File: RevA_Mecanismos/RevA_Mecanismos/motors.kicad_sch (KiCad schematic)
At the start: 46 parts, among them U4 TXU0304PWR, U6 SRV05-4

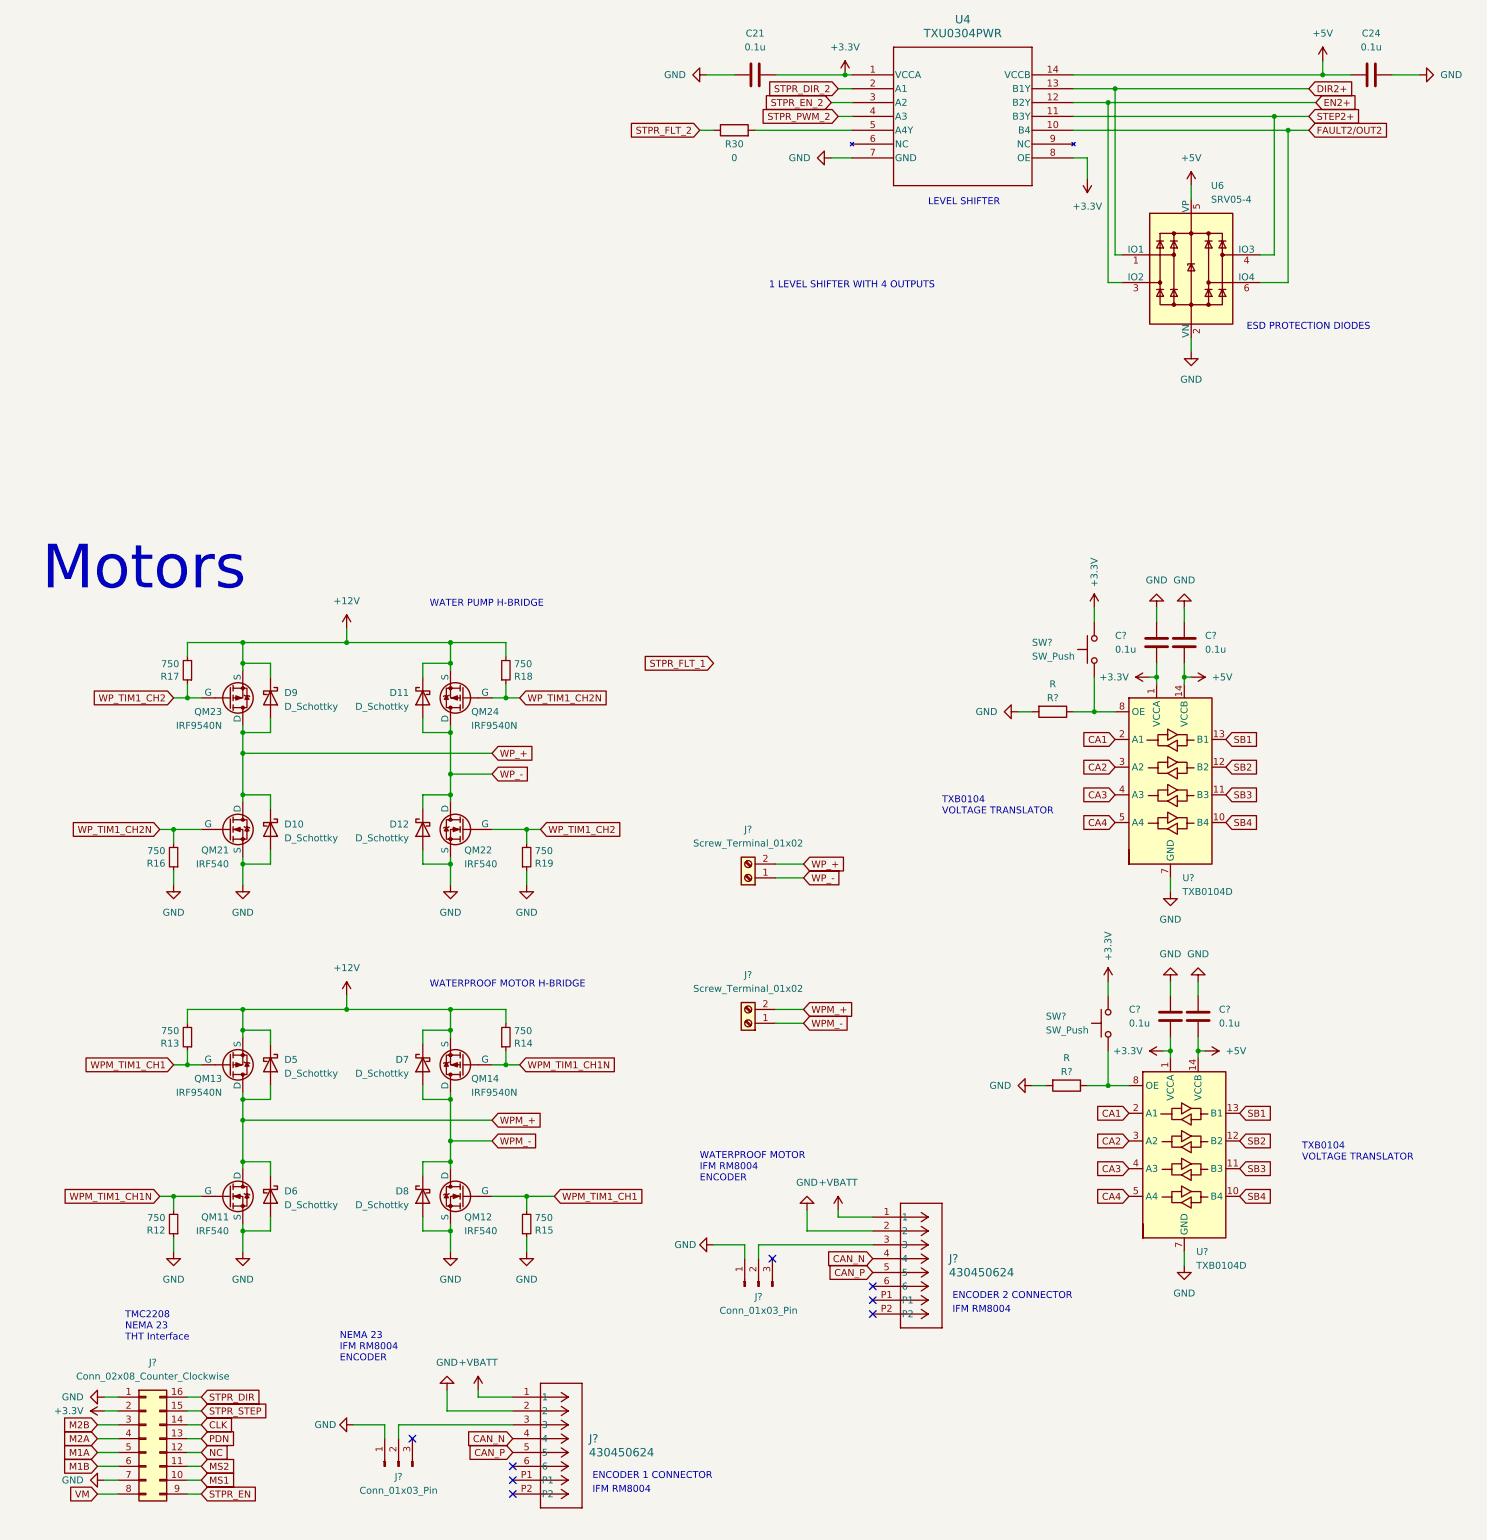
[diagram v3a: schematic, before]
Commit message: Debug connectors and pwr flag to +12v
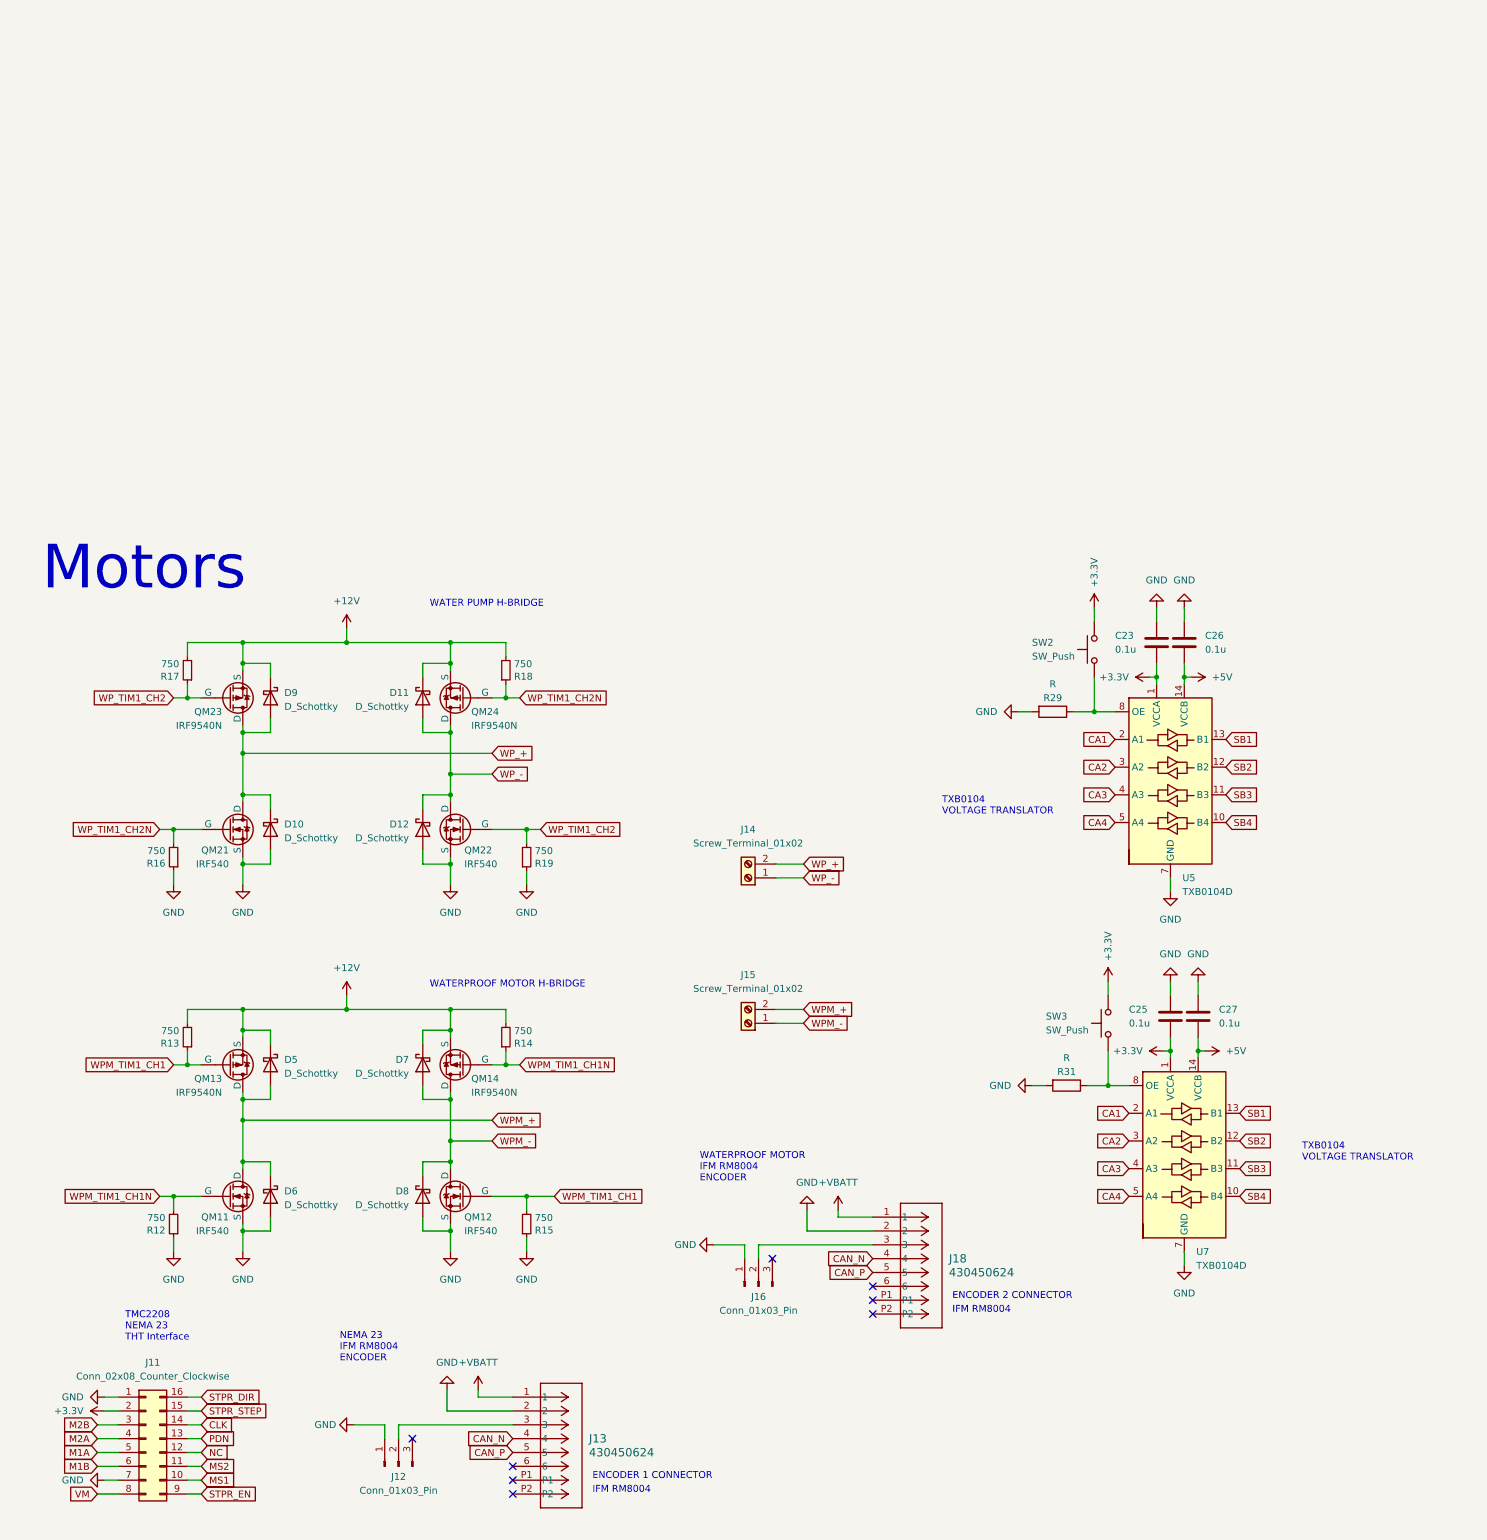
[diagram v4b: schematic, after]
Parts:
- removed C21, C24: 0.1u, symbol Device:C
- removed R30: 0, symbol Device:R
- removed U4: TXU0304PWR, TSSOP14_PW_TEX, symbol TXU0304PWR:TXU0304PWR
- removed U6: SRV05-4, Package_TO_SOT_SMD:SOT-23-6, symbol Power_Protection:SRV05-4
- gave numbers to parts that had none: 17
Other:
- note removed: "1 LEVEL SHIFTER WITH 4 OUTPUTS"
- note removed: "ESD PROTECTION DIODES"
- note removed: "LEVEL SHIFTER"

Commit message: Updated STM32 USV Mechanism PCB
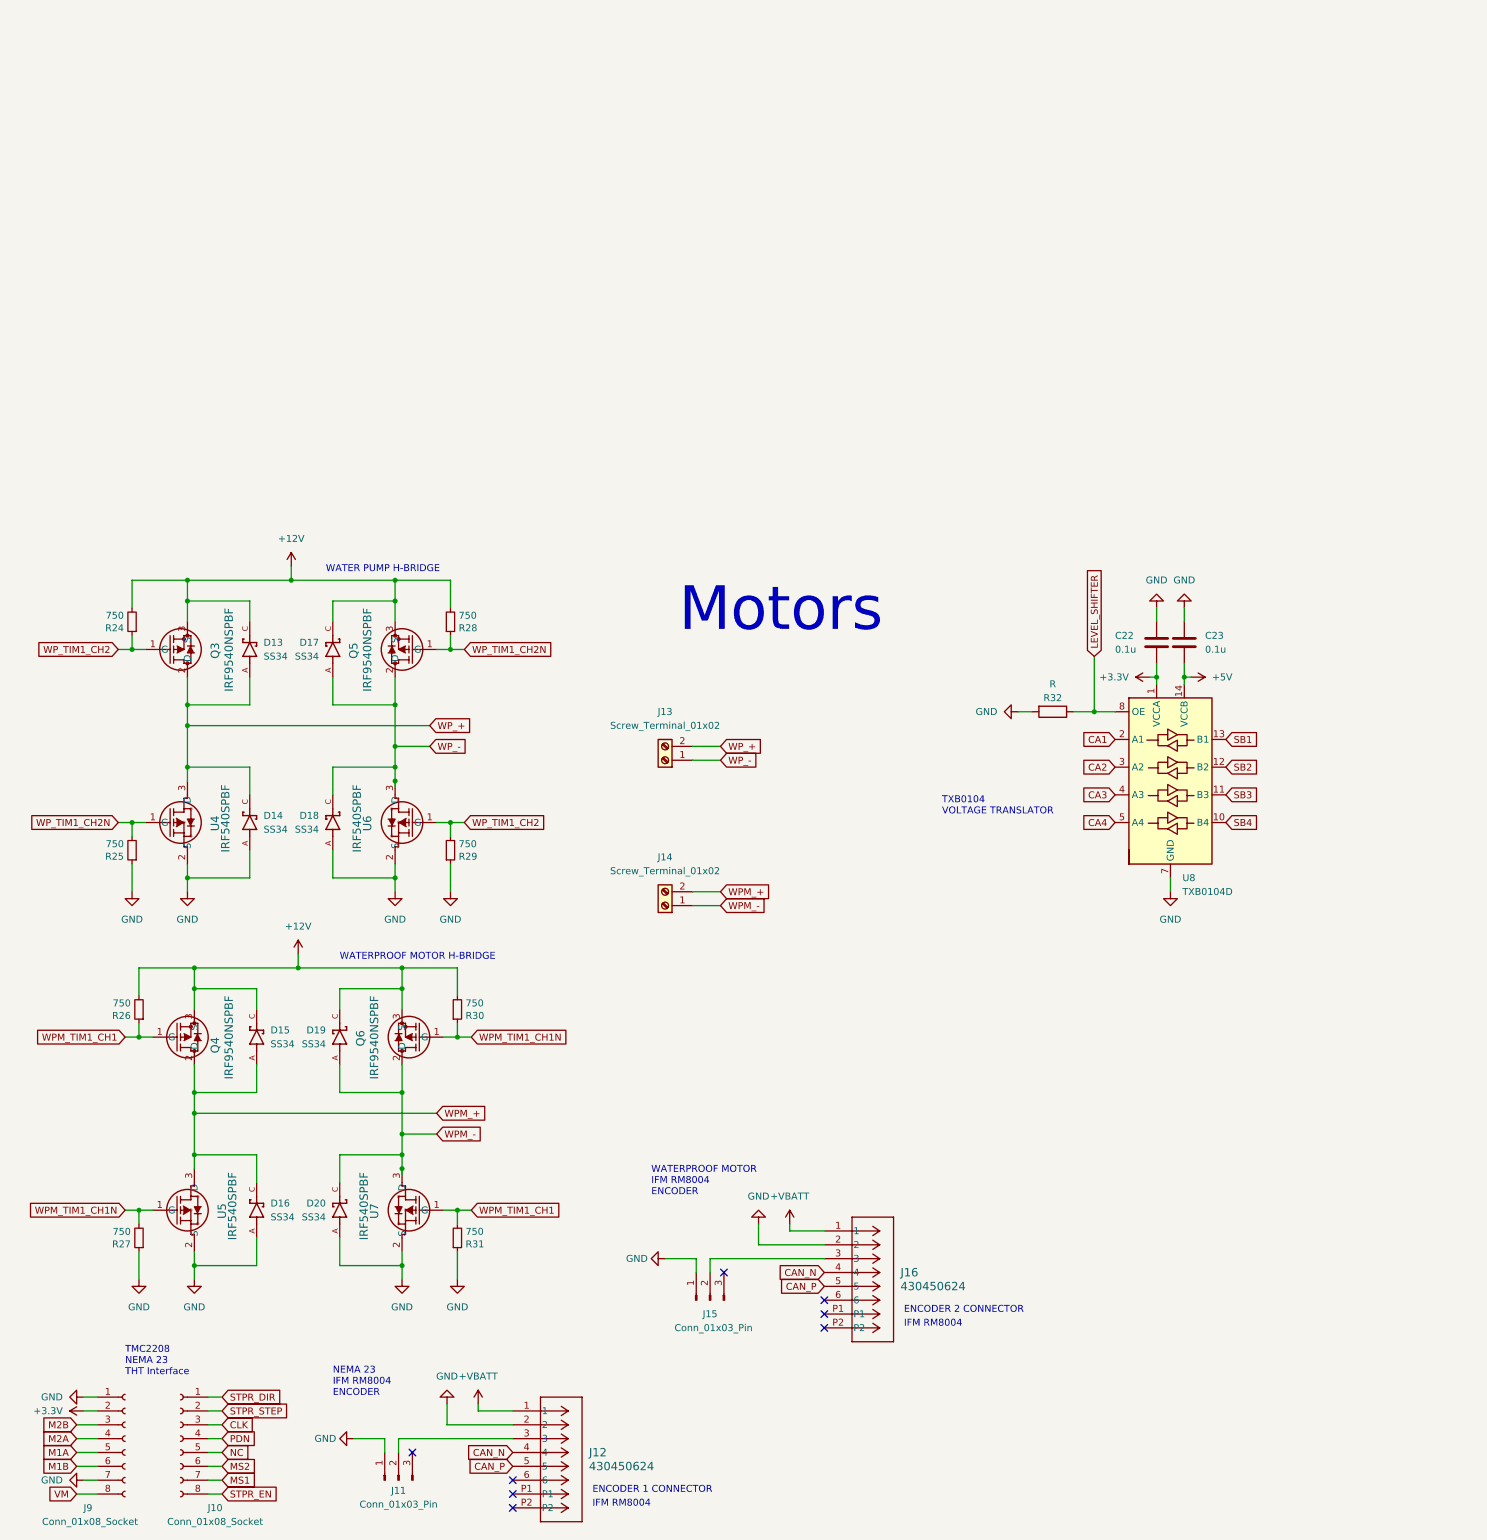
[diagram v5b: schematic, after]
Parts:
- removed C25, C27: 0.1u, symbol Device:C
- removed D10, D11, D12, D5, D6, D7, D8, D9: D_Schottky, symbol Device:D_Schottky
- removed J11: Conn_02x08_Counter_Clockwise, Connector_PinHeader_2.54mm:PinHeader_2x08_P2.54mm_Vertical, symbol Connector_Generic:Conn_02x08_Counter_Clockwise
- removed QM11, QM12, QM21, QM22: IRF540, symbol Simulation_SPICE:NMOS
- removed QM13, QM14, QM23, QM24: IRF9540N, symbol Simulation_SPICE:PMOS
- removed R12, R13, R14, R15, R16, R17, R18, R19: 750, Resistor_SMD:R_0603_1608Metric, symbol Device:R_Small
- removed R31: R, symbol Device:R
- removed SW2, SW3: SW_Push, symbol Switch:SW_Push
- removed U7: TXB0104D, Package_SO:SOIC-14_3.9x8.7mm_P1.27mm, symbol Logic_LevelTranslator:TXB0104D
- added D13, D14, D15, D16, D17, D18, D19, D20: SS34, SS34:SS34, symbol SS34:SS34
- added J10, J9: Conn_01x08_Socket, Connector_PinSocket_2.54mm:PinSocket_1x08_P2.54mm_Vertical, symbol Connector:Conn_01x08_Socket
- added Q3, Q4, Q5, Q6: IRF9540NSPBF, PMOSGDS_D2PAK_INF, symbol IRF9540NSPBF:IRF9540NSPBF
- added R24, R25, R26, R27, R28, R29, R30, R31: 750, Resistor_SMD:R_0603_1608Metric, symbol Device:R_Small
- added U4, U5, U6, U7: IRF540SPBF, D2PAK_VIS, symbol IRF540SPBF:IRF540SPBF
- C22: renamed from C23; footprint (none) -> Capacitor_SMD:C_0603_1608Metric
- C23: renamed from C26; footprint (none) -> Capacitor_SMD:C_0603_1608Metric
- J11: renamed from J12; footprint (none) -> Connector_PinHeader_2.54mm:PinHeader_1x03_P2.54mm_Vertical
- J12: renamed from J13; footprint CON_430450624_MOL -> MolexConnectors:CON_430450624_MOL
- J15: renamed from J16; footprint (none) -> Connector_PinHeader_2.54mm:PinHeader_1x03_P2.54mm_Vertical
- J16: renamed from J18; footprint CON_430450624_MOL -> MolexConnectors:CON_430450624_MOL
- R32: renamed from R29; footprint (none) -> Resistor_SMD:R_0603_1608Metric
- renumbered J14 to J13, J15 to J14, U5 to U8
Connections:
- net +12V: now also D13.C, D15.C, D17.C, D19.C, Q3.3 (S), Q4.3 (S), Q5.3 (S), Q6.3 (S), R24.2, R26.2, R28.2, R30.2
- net +3.3V: now also J9.2 (Pin_2)
- net CLK: now also J10.3 (Pin_3)
- net GND: now also D14.A, D16.A, D18.A, D20.A, J9.1 (Pin_1), J9.7 (Pin_7), R25.1, R27.1, R29.1, R31.1, U4.2 (S), U5.2 (S), U6.2 (S), U7.2 (S)
- net M1A: now also J9.5 (Pin_5)
- net M1B: now also J9.6 (Pin_6)
- net M2A: now also J9.4 (Pin_4)
- net M2B: now also J9.3 (Pin_3)
- net MS1: now also J10.7 (Pin_7)
- net MS2: now also J10.6 (Pin_6)
- net NC: now also J10.5 (Pin_5)
- net PDN: now also J10.4 (Pin_4)
- net STPR_DIR: now also J10.1 (Pin_1)
- net STPR_EN: now also J10.8 (Pin_8)
- net STPR_STEP: now also J10.2 (Pin_2)
- net VM: now also J9.8 (Pin_8)
- net WPM_+: now also D15.A, D16.C, Q4.2 (D), U5.3 (D)
- net WPM_-: now also D19.A, D20.C, Q6.2 (D), U7.3 (D)
- net WPM_TIM1_CH1: now also Q4.1 (G), R26.1, R31.2, U7.1 (G)
- net WPM_TIM1_CH1N: now also Q6.1 (G), R27.2, R30.1, U5.1 (G)
- net WP_+: now also D13.A, D14.C, Q3.2 (D), U4.3 (D)
- net WP_-: now also D17.A, D18.C, Q5.2 (D), U6.3 (D)
- net WP_TIM1_CH2: now also Q3.1 (G), R24.1, R29.2, U6.1 (G)
- net WP_TIM1_CH2N: now also Q5.1 (G), R25.2, R28.1, U4.1 (G)
- net LEVEL_SHIFTER: now reaches R32.1, U8.8 (OE)
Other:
- moved on the sheet: J11, J12, J13, J14, J15, J16
